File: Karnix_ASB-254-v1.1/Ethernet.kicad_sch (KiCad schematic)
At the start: 56 parts, among them U8 LAN8710AI

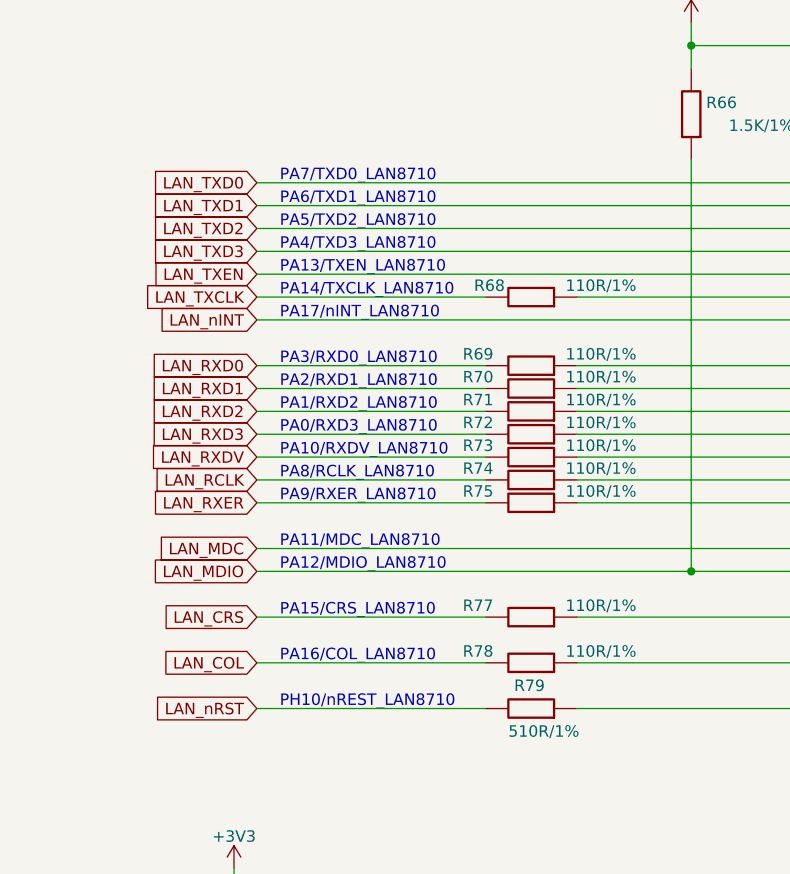
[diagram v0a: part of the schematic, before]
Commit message: Remove rudimentary signal names for Ethernet
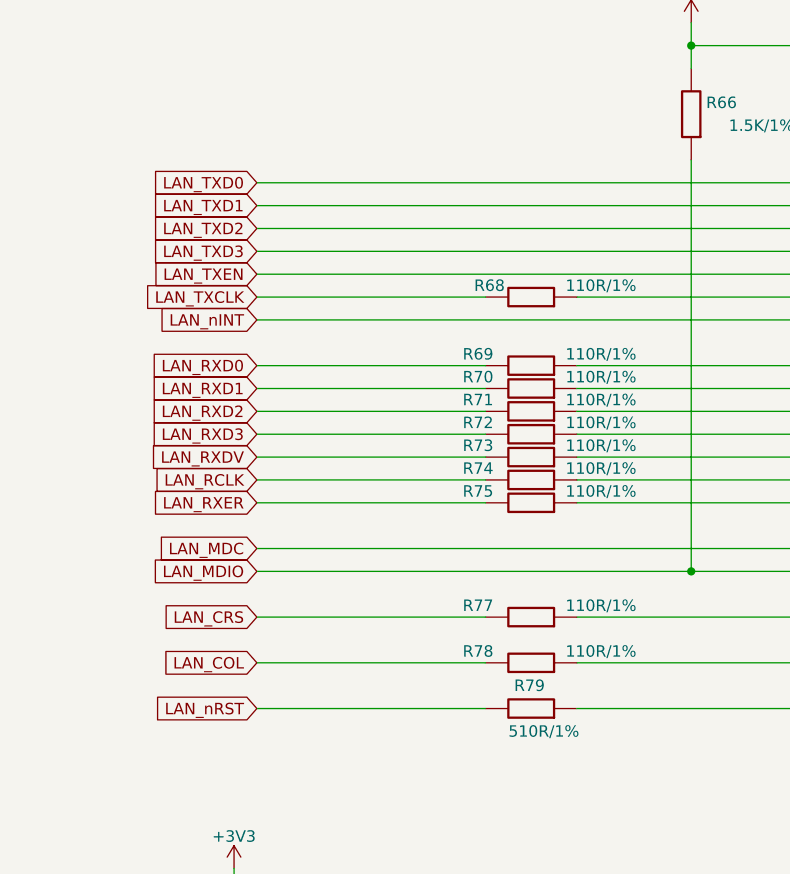
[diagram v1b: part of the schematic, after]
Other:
- note removed: "PA0/RXD3_LAN8710"
- note removed: "PA1/RXD2_LAN8710"
- note removed: "PA10/RXDV_LAN8710"
- note removed: "PA11/MDC_LAN8710"
- note removed: "PA12/MDIO_LAN8710"
- note removed: "PA13/TXEN_LAN8710"
- note removed: "PA14/TXCLK_LAN8710"
- note removed: "PA15/CRS_LAN8710"
- note removed: "PA16/COL_LAN8710"
- note removed: "PA17/nINT_LAN8710"
- note removed: "PA2/RXD1_LAN8710"
- note removed: "PA3/RXD0_LAN8710"
- note removed: "PA4/TXD3_LAN8710"
- note removed: "PA5/TXD2_LAN8710"
- note removed: "PA6/TXD1_LAN8710"
- note removed: "PA7/TXD0_LAN8710"
- note removed: "PA8/RCLK_LAN8710"
- note removed: "PA9/RXER_LAN8710"
- note removed: "PH10/nREST_LAN8710"
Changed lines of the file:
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@@
     (stroke (width 0) (type default))
-  )
-  (text "PA17/nINT_LAN8710" (at 50.165 71.12 0)
-    (effects (font (size 1.27 1.27)) (justify left bottom))
-  )
-  (text "PA12/MDIO_LAN8710" (at 50.165 99.06 0)
-    (effects (font (size 1.27 1.27)) (justify left bottom))
-  )
-  (text "PA0/RXD3_LAN8710" (at 50.165 83.82 0)
-    (effects (font (size 1.27 1.27)) (justify left bottom))
-  )
-  (text "PA15/CRS_LAN8710" (at 50.165 104.14 0)
-    (effects (font (size 1.27 1.27)) (justify left bottom))
-  )
-  (text "PA14/TXCLK_LAN8710" (at 50.165 68.58 0)
-    (effects (font (size 1.27 1.27)) (justify left bottom))
-  )
-  (text "PA4/TXD3_LAN8710" (at 50.165 63.5 0)
-    (effects (font (size 1.27 1.27)) (justify left bottom))
-  )
-  (text "PA8/RCLK_LAN8710" (at 50.165 88.9 0)
-    (effects (font (size 1.27 1.27)) (justify left bottom))
-  )
-  (text "PA6/TXD1_LAN8710" (at 50.165 58.42 0)
-    (effects (font (size 1.27 1.27)) (justify left bottom))
-  )
-  (text "PA3/RXD0_LAN8710" (at 50.165 76.2 0)
-    (effects (font (size 1.27 1.27)) (justify left bottom))
-  )
-  (text "PA2/RXD1_LAN8710" (at 50.165 78.74 0)
-    (effects (font (size 1.27 1.27)) (justify left bottom))
-  )
-  (text "PA13/TXEN_LAN8710" (at 50.165 66.04 0)
-    (effects (font (size 1.27 1.27)) (justify left bottom))
   )
   (text "Passove PoE" (at 46 213 0)
     (effects (font (size 1.27 1.27)) (justify left bottom))
   )
-  (text "PA11/MDC_LAN8710" (at 50.165 96.52 0)
-    (effects (font (size 1.27 1.27)) (justify left bottom))
-  )
-  (text "PA5/TXD2_LAN8710" (at 50.165 60.96 0)
-    (effects (font (size 1.27 1.27)) (justify left bottom))
-  )
-  (text "PA9/RXER_LAN8710" (at 50.165 91.44 0)
-    (effects (font (size 1.27 1.27)) (justify left bottom))
-  )
-  (text "PA7/TXD0_LAN8710" (at 50.165 55.88 0)
-    (effects (font (size 1.27 1.27)) (justify left bottom))
-  )
-  (text "PA10/RXDV_LAN8710" (at 50.165 86.36 0)
-    (effects (font (size 1.27 1.27)) (justify left bottom))
-  )
-  (text "PH10/nREST_LAN8710" (at 50.165 114.3 0)
-    (effects (font (size 1.27 1.27)) (justify left bottom))
-  )
-  (text "PA1/RXD2_LAN8710" (at 50.165 81.28 0)
-    (effects (font (size 1.27 1.27)) (justify left bottom))
-  )
-  (text "PA16/COL_LAN8710" (at 50.165 109.22 0)
-    (effects (font (size 1.27 1.27)) (justify left bottom))
-  )

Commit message: Substitute +3V3_ETH with +3V3 through ferrite bead
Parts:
- added L17: 330R/1.2A, Inductor_SMD:L_0603_1608Metric, symbol Fabmicro:Ferrite_Beads
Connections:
- net +3V3: now also L17.2
- net +3V3_ETH: no longer names the net of R100.1, R96.1, R97.1, R98.1, R99.1
- net +3V3_ETH: now also L17.1
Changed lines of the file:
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@@
   (junction (at 217.805 185.42) (diameter 0) (color 0 0 0 0)
   )
-  (junction (at 207.645 185.42) (diameter 0) (color 0 0 0 0)
-  )
   (junction (at 55.245 134.62) (diameter 0) (color 0 0 0 0)
   )
@@
   (junction (at 45.085 134.62) (diameter 0) (color 0 0 0 0)
   )
+  (junction (at 207.645 185.42) (diameter 0) (color 0 0 0 0)
+  )
   (junction (at 95.885 99.06) (diameter 0) (color 0 0 0 0)
   )
@@
     (stroke (width 0) (type default))
   )
+  (wire (pts (xy 193.802 182.88) (xy 193.802 185.42))
+    (stroke (width 0) (type default))
+  )
   (wire (pts (xy 238.125 185.42) (xy 248.285 185.42))
     (stroke (width 0) (type default))
@@
     (stroke (width 0) (type default))
   )
+  (wire (pts (xy 193.802 185.42) (xy 197.485 185.42))
+    (stroke (width 0) (type default))
+  )
   (wire (pts (xy 233.045 88.9) (xy 233.045 86.36))
     (stroke (width 0) (type default))
@@
     (stroke (width 0) (type default))
   )
-  (wire (pts (xy 207.645 185.42) (xy 207.645 182.88))
-    (stroke (width 0) (type default))
-  )
   (wire (pts (xy 197.485 203.2) (xy 217.805 203.2))
     (stroke (width 0) (type default))
@@
     )
   )
-  (symbol (lib_id "Fabmicro:+3V3_ETH") (at 207.645 182.88 0) (unit 1)
-    (in_bom yes) (on_board yes) (dnp no)
-    (property "Reference" "#PWR0127" (at 207.645 186.69 0)
-      (effects (font (size 1.27 1.27)) hide)
-    )
-    (property "Value" "+3V3_ETH" (at 207.645 179.07 0)
-      (effects (font (size 1.27 1.27)))
-    )
-    (property "Footprint" "" (at 207.645 182.88 0)
-      (effects (font (size 1.27 1.27)) hide)
-    )
-    (property "Datasheet" "" (at 207.645 182.88 0)
-      (effects (font (size 1.27 1.27)) hide)
-    )
-    (pin "1")
-    (instances
-      (project "Karnix_ASB"
-        (path "/fe37e245-9527-4c72-91fc-09b617a42f73/00000000-0000-0000-0000-0000602e11fa"
-          (reference "#PWR0127") (unit 1)
-        )
-      )
-    )
-  )
   (symbol (lib_id "power:GND") (at 212.725 66.04 0) (unit 1)
     (in_bom yes) (on_board yes) (dnp no)
@@
         )
       )
+    )
+  )
+  (symbol (lib_id "Fabmicro:Ferrite_Beads") (at 202.565 185.42 0) (mirror y) (unit 1)
+    (in_bom yes) (on_board yes) (dnp no)
+    (property "Reference" "L17" (at 202.565 182.245 0)
+      (effects (font (size 1.27 1.27)))
+    )
+    (property "Value" "330R/1.2A" (at 202.565 187.96 0)
+      (effects (font (size 1.27 1.27)))
+    )
+    (property "Footprint" "Inductor_SMD:L_0603_1608Metric" (at 202.565 185.42 90)
+      (effects (font (size 1.27 1.27)) hide)
+    )
+    (property "Datasheet" "" (at 202.565 185.42 90)
+      (effects (font (size 1.27 1.27)) hide)
+    )
+    (property "PN" "" (at 202.565 185.42 0)
+      (effects (font (size 1.27 1.27)) hide)
+    )
+    (property "Mfr. Part Number" "BLM18PG331SN1D" (at 202.565 185.42 0)
+      (effects (font (size 1.27 1.27)) hide)
+    )
+    (property "Supplier" "Fabmicro" (at 202.565 185.42 0)
+      (effects (font (size 1.27 1.27)) hide)
+    )
+    (pin "1")
+    (pin "2")
+    (instances
+      (project "Karnix_ASB"
+        (path "/fe37e245-9527-4c72-91fc-09b617a42f73/00000000-0000-0000-0000-0000602e11fa"
+          (reference "L17") (unit 1)
+        )
+      )
+    )
+  )
+  (symbol (lib_id "Fabmicro:+3V3") (at 193.802 182.88 0) (unit 1)
+    (in_bom yes) (on_board yes) (dnp no) (fields_autoplaced)
+    (property "Reference" "#PWR050" (at 193.802 186.69 0)
+      (effects (font (size 1.27 1.27)) hide)
+    )
+    (property "Value" "+3V3" (at 193.802 179.3129 0)
+      (effects (font (size 1.27 1.27)))
+    )
+    (property "Footprint" "" (at 193.802 182.88 0)
+      (effects (font (size 1.27 1.27)) hide)
+    )
+    (property "Datasheet" "" (at 193.802 182.88 0)
+      (effects (font (size 1.27 1.27)) hide)
+    )
+    (pin "1")
+    (instances
+      (project "Karnix_ASB"
+        (path "/fe37e245-9527-4c72-91fc-09b617a42f73/00000000-0000-0000-0000-0000602e0fd3"
+          (reference "#PWR050") (unit 1)
+        )
+        (path "/fe37e245-9527-4c72-91fc-09b617a42f73/00000000-0000-0000-0000-0000602e11fa"
+          (reference "#PWR0127") (unit 1)
+        )
+      )
